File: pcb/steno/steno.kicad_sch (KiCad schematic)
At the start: 53 parts, among them J1 Conn_01x04, K1 diode-choc, K10 diode-choc, K11 diode-choc, K12 diode-choc, K13 diode-choc, K14 diode-choc, K15 diode-choc, K16 diode-choc, K17 diode-choc, K18 diode-choc, K19 diode-choc, K2 diode-choc, K20 diode-choc, K21 diode-choc, K22 diode-choc, K23 diode-choc, K24 diode-choc, K25 diode-choc, K26 diode-choc, K27 diode-choc, K28 diode-choc, K29 diode-choc, K3 diode-choc, K30 diode-choc, K4 diode-choc, K5 diode-choc, K6 diode-choc, K7 diode-choc, K8 diode-choc, K9 diode-choc, Q1 AO3401A, SW2 SW_Push, U1 MT25QL128ABA1ESE, U2 LCD2.2in, U3 Holyiot_18010_no_underside

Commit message: [pcb] Auklet 3
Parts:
- added K32, K33, K34, K35, K36, K38, K39, K40, K41, K42: diode-choc, pg1350:pg1350-D, symbol diode-choc:diode-choc
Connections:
- net C2: now also K32.2, K38.2
- net C3: now also K33.2, K39.2
- net C4: now also K34.2, K40.2
- net C5: now also K35.2, K41.2
- net C6: now also K36.2, K42.2
- net R3: now also K32.1, K33.1, K34.1, K35.1, K36.1; no longer K13.1, K14.1, K15.1, K16.1, K17.1, K18.1, U3.43 (P0.22)
- net R4: now also K13.1, K14.1, K15.1, K16.1, K17.1, K18.1, U3.43 (P0.22); no longer K19.1, K20.1, K21.1, K22.1, K23.1, K24.1, U3.41 ([L]_P1.03)
- net R5: now also K19.1, K20.1, K21.1, K22.1, K23.1, K24.1, U3.41 ([L]_P1.03); no longer K25.1, K26.1, K27.1, K28.1, K29.1, K30.1, U3.42 (P1.00)
- new net R6: K25.1, K26.1, K27.1, K28.1, K29.1, K30.1, U3.42 (P1.00)
- new net R7: K38.1, K39.1, K40.1, K41.1, K42.1
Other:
- moved on the sheet: K1, K10, K11, K12, K13, K14, K15, K16, K17, K18, K19, K2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

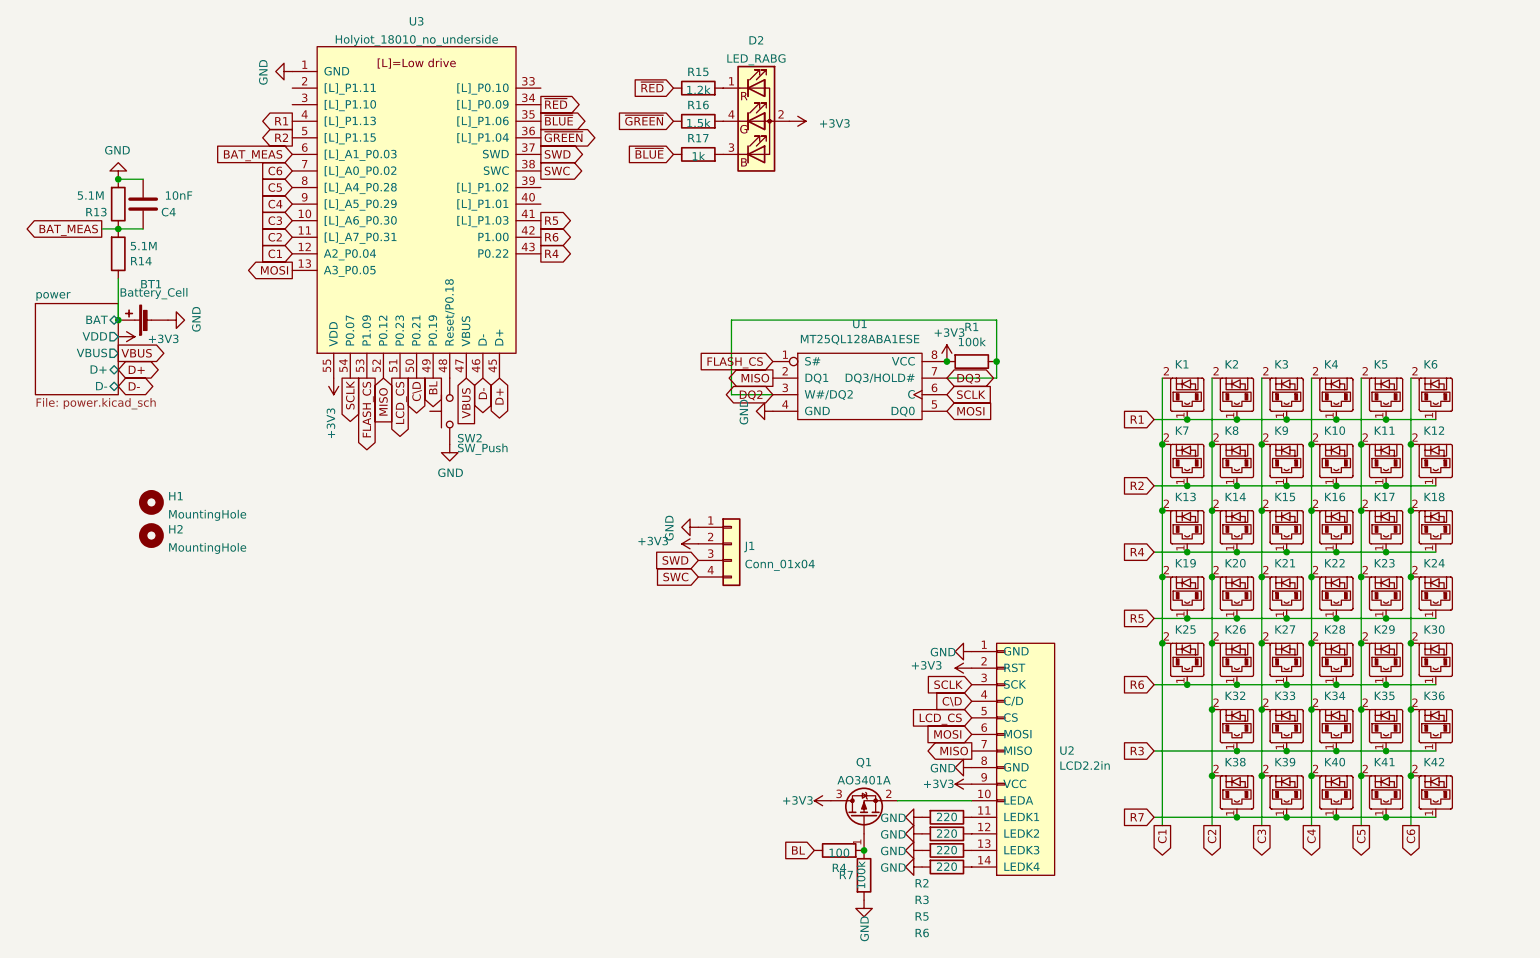
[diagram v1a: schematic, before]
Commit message: [pcb] auklet 3: use new libraries
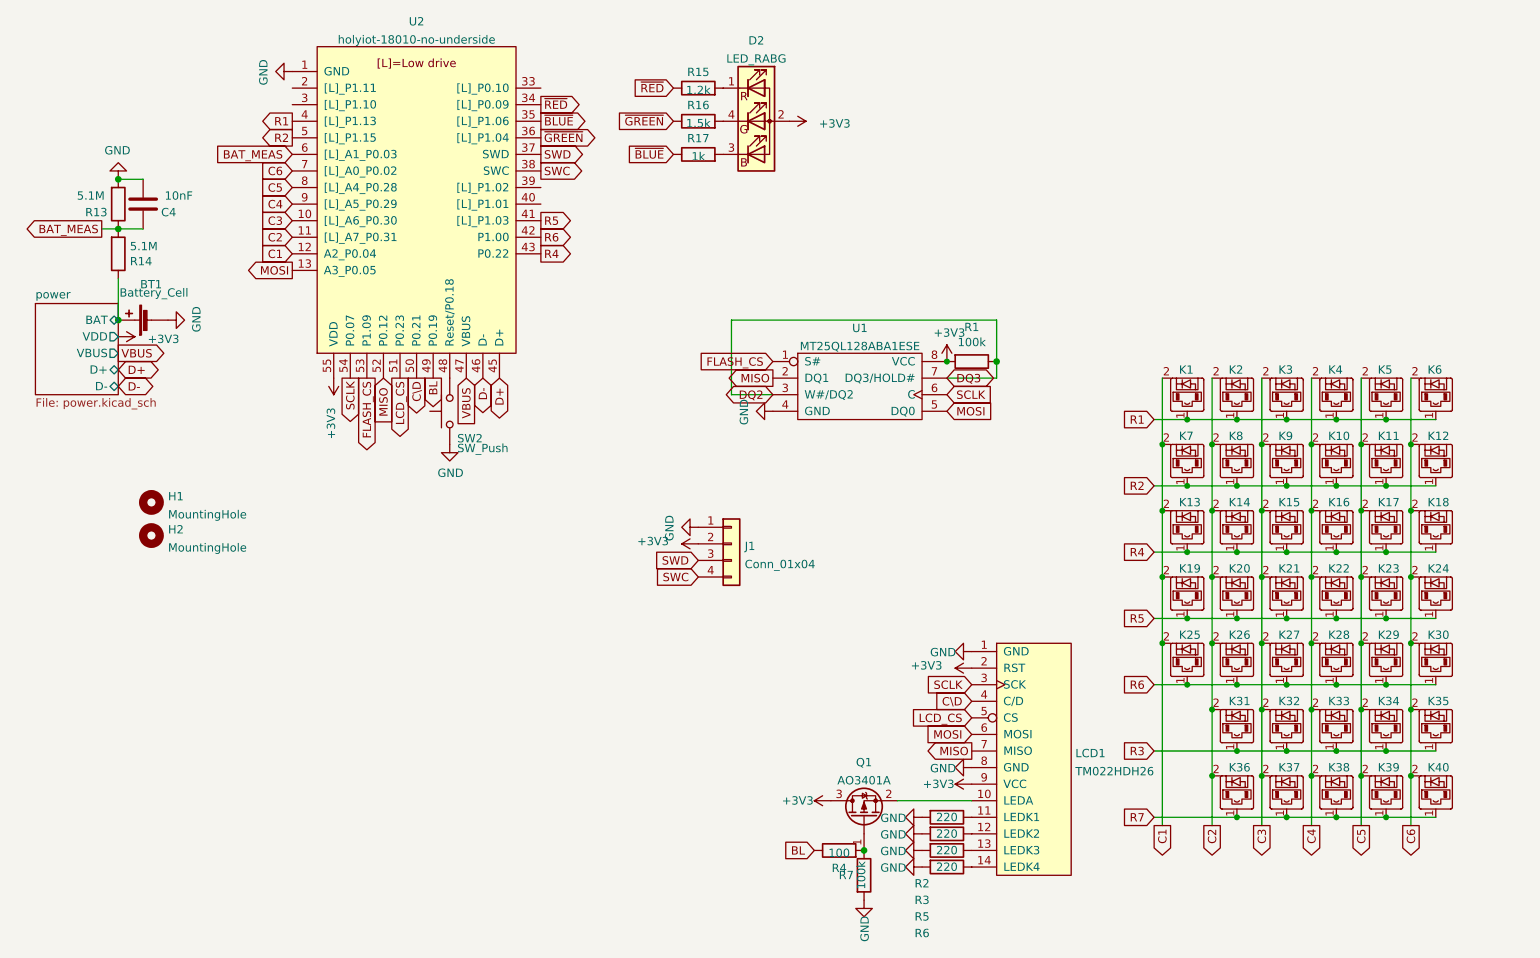
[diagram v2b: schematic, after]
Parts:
- removed K41, K42: diode-choc, pg1350:pg1350-D, symbol diode-choc:diode-choc
- removed U1: MT25QL128ABA1ESE, Package_SO:SOP-8_5.28x5.23mm_P1.27mm, symbol steno:MT25QL128ABA1ESE
- removed U2: LCD2.2in, misc:TM022HDH26, symbol steno:LCD2.2in
- removed U3: Holyiot_18010_no_underside, keeb-libs:Holyiot-18010-no-underside, symbol keeb-libs:Holyiot_18010_no_underside
- added K31, K37: diode-choc, pg1350:pg1350-D, symbol diode-choc:diode-choc
- added LCD1: TM022HDH26, display:TM022HDH26, symbol display:TM022HDH26
- added U1: MT25QL128ABA1ESE, Package_SO:SOIC-8_5.23x5.23mm_P1.27mm, symbol ic:MT25QL128ABA1ESE
- added U2: holyiot-18010-no-underside, mcu:Holyiot-18010-no-underside, symbol mcu:holyiot-18010-no-underside
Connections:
- net +3V3: now also LCD1.2 (RST), LCD1.9 (VCC), U1.8 (VCC), U2.55 (VDD)
- net BAT_MEAS: now also U2.6 ([L]_A1_P0.03)
- net BL: now also U2.49 (P0.19)
- net C1: now also U2.12 (A2_P0.04)
- net C2: now also K36.2, K31.2, U2.11 ([L]_A7_P0.31); no longer K32.2, K38.2
- net C3: now also K32.2, K37.2, U2.10 ([L]_A6_P0.30); no longer K33.2, K39.2
- net C4: now also K33.2, K38.2, U2.9 ([L]_A5_P0.29); no longer K34.2, K40.2
- net C5: now also K34.2, K39.2, U2.8 ([L]_A4_P0.28); no longer K35.2
- net C6: now also K35.2, K40.2, U2.7 ([L]_A0_P0.02); no longer K36.2
- net C\D: now also LCD1.4 (C/D), U2.50 (P0.21)
- net D+: now also U2.45 (D+)
- net D-: now also U2.46 (D-)
- net DQ2: now also U1.3 (W#/DQ2), U1.7 (DQ3/HOLD#)
- net FLASH_CS: now also U1.1 (S#), U2.53 (P1.09)
- net GND: now also LCD1.1 (GND), LCD1.8 (GND), U1.4 (GND), U2.1 (GND), U2.32 (GND), U2.44 (GND)
- net LCD_CS: now also LCD1.5 (CS), U2.51 (P0.23)
- net MISO: now also LCD1.7 (MISO), U1.2 (DQ1), U2.52 (P0.12)
- net MOSI: now also LCD1.6 (MOSI), U1.5 (DQ0), U2.13 (A3_P0.05)
- net R1: now also U2.4 ([L]_P1.13)
- net R2: now also U2.5 ([L]_P1.15)
- net R3: now also K31.1; no longer K36.1
- net R4: now also U2.43 (P0.22)
- net R5: now also U2.41 ([L]_P1.03)
- net R6: now also U2.42 (P1.00)
- net R7: now also K36.1, K37.1
- net SCLK: now also LCD1.3 (SCK), U1.6 (C), U2.54 (P0.07)
- net SWC: now also U2.38 (SWC)
- net SWD: now also U2.37 (SWD)
- net VBUS: now also U2.47 (VBUS)
- net ~{BLUE}: now also U2.35 ([L]_P1.06)
- net ~{GREEN}: now also U2.36 ([L]_P1.04)
- net ~{RED}: now also U2.34 ([L]_P0.09)
- net at Q1.2 (S): now also LCD1.10 (LEDA)
- net at R2.1: now also LCD1.11 (LEDK1)
- net at R3.1: now also LCD1.12 (LEDK2)
- net at R5.1: now also LCD1.13 (LEDK3)
- net at R6.1: now also LCD1.14 (LEDK4)
- net at SW2.2: now also U2.48 (Reset/P0.18)

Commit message: [pcb] Auklet 3: first revision
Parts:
- removed J1: Conn_01x04, keeb-libs:debug-port-single-side, symbol Connector_Generic:Conn_01x04
- added J1: debug-port, misc:debug-port-single-side, symbol misc:debug-port
- U2: footprint mcu:Holyiot-18010-no-underside -> mcu:holyiot-18010-no-underside
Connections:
- net +3V3: now also J1.2 (3V3)
- net GND: now also J1.1 (GND)
- net SWC: now also J1.4 (SWC)
- net SWD: now also J1.3 (SWD)
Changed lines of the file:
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@@
     )
   )
-  (global_label "SWD" (shape input) (at 119.38 110.49 180) (fields_autoplaced)
-    (effects (font (size 1.27 1.27)) (justify right))
-    (property "Intersheet References" "${INTERSHEET_REFS}" (id 0) (at 113.0359 110.4106 0)
-      (effects (font (size 1.27 1.27)) (justify right) hide)
-    )
-  )
-  (global_label "SWC" (shape input) (at 119.38 113.03 180) (fields_autoplaced)
-    (effects (font (size 1.27 1.27)) (justify right))
-    (property "Intersheet References" "${INTERSHEET_REFS}" (id 0) (at 113.0359 112.9506 0)
+  (global_label "SWD" (shape input) (at 128.27 120.65 180) (fields_autoplaced)
+    (effects (font (size 1.27 1.27)) (justify right))
+    (property "Intersheet References" "${INTERSHEET_REFS}" (id 0) (at 121.9259 120.5706 0)
+      (effects (font (size 1.27 1.27)) (justify right) hide)
+    )
+  )
+  (global_label "SWC" (shape input) (at 128.27 118.11 180) (fields_autoplaced)
+    (effects (font (size 1.27 1.27)) (justify right))
+    (property "Intersheet References" "${INTERSHEET_REFS}" (id 0) (at 121.9259 118.0306 0)
       (effects (font (size 1.27 1.27)) (justify right) hide)
     )
@@
     (pin "2")
   )
-  (symbol (lib_id "power:+3V3") (at 119.38 107.95 90) (unit 1)
-    (in_bom yes) (on_board yes)
-    (property "Reference" "#PWR06" (id 0) (at 123.19 107.95 0)
-      (effects (font (size 1.27 1.27)) hide)
-    )
-    (property "Value" "+3V3" (id 1) (at 112.4458 107.569 90))
-    (property "Footprint" "" (id 2) (at 119.38 107.95 0)
-      (effects (font (size 1.27 1.27)) hide)
-    )
-    (property "Datasheet" "" (id 3) (at 119.38 107.95 0)
+  (symbol (lib_id "power:+3V3") (at 128.27 123.19 90) (unit 1)
+    (in_bom yes) (on_board yes)
+    (property "Reference" "#PWR06" (id 0) (at 132.08 123.19 0)
+      (effects (font (size 1.27 1.27)) hide)
+    )
+    (property "Value" "+3V3" (id 1) (at 121.3358 122.809 90))
+    (property "Footprint" "" (id 2) (at 128.27 123.19 0)
+      (effects (font (size 1.27 1.27)) hide)
+    )
+    (property "Datasheet" "" (id 3) (at 128.27 123.19 0)
       (effects (font (size 1.27 1.27)) hide)
     )
@@
     (property "Reference" "U2" (id 0) (at 76.2 27.9105 0))
     (property "Value" "holyiot-18010-no-underside" (id 1) (at 76.2 30.6856 0))
-    (property "Footprint" "mcu:Holyiot-18010-no-underside" (id 2) (at 114.3 73.66 0)
+    (property "Footprint" "mcu:holyiot-18010-no-underside" (id 2) (at 114.3 73.66 0)
       (effects (font (size 1.27 1.27)) hide)
     )
@@
     (pin "2")
   )
-  (symbol (lib_id "power:GND") (at 119.38 105.41 270) (unit 1)
-    (in_bom yes) (on_board yes)
-    (property "Reference" "#PWR05" (id 0) (at 113.03 105.41 0)
-      (effects (font (size 1.27 1.27)) hide)
-    )
-    (property "Value" "GND" (id 1) (at 114.9858 105.537 0))
-    (property "Footprint" "" (id 2) (at 119.38 105.41 0)
-      (effects (font (size 1.27 1.27)) hide)
-    )
-    (property "Datasheet" "" (id 3) (at 119.38 105.41 0)
+  (symbol (lib_id "misc:debug-port") (at 132.08 121.92 90) (unit 1)
+    (in_bom no) (on_board yes) (fields_autoplaced)
+    (property "Reference" "J1" (id 0) (at 136.525 121.0115 90)
+      (effects (font (size 1.27 1.27)) (justify right))
+    )
+    (property "Value" "debug-port" (id 1) (at 136.525 123.7866 90)
+      (effects (font (size 1.27 1.27)) (justify right))
+    )
+    (property "Footprint" "misc:debug-port-single-side" (id 2) (at 139.7 121.92 0)
+      (effects (font (size 1.27 1.27)) hide)
+    )
+    (property "Datasheet" "" (id 3) (at 132.08 121.92 0)
+      (effects (font (size 1.27 1.27)) hide)
+    )
+    (pin "1")
+    (pin "2")
+    (pin "3")
+    (pin "4")
+  )
+  (symbol (lib_id "power:GND") (at 128.27 125.73 270) (unit 1)
+    (in_bom yes) (on_board yes)
+    (property "Reference" "#PWR05" (id 0) (at 121.92 125.73 0)
+      (effects (font (size 1.27 1.27)) hide)
+    )
+    (property "Value" "GND" (id 1) (at 123.8758 125.857 0))
+    (property "Footprint" "" (id 2) (at 128.27 125.73 0)
+      (effects (font (size 1.27 1.27)) hide)
+    )
+    (property "Datasheet" "" (id 3) (at 128.27 125.73 0)
       (effects (font (size 1.27 1.27)) hide)
     )
@@
     (pin "1")
     (pin "2")
-  )
-  (symbol (lib_id "Connector_Generic:Conn_01x04") (at 124.46 107.95 0) (unit 1)
-    (in_bom yes) (on_board yes) (fields_autoplaced)
-    (property "Reference" "J1" (id 0) (at 126.4921 108.3115 0)
-      (effects (font (size 1.27 1.27)) (justify left))
-    )
-    (property "Value" "Conn_01x04" (id 1) (at 126.4921 111.0866 0)
-      (effects (font (size 1.27 1.27)) (justify left))
-    )
-    (property "Footprint" "keeb-libs:debug-port-single-side" (id 2) (at 124.46 107.95 0)
-      (effects (font (size 1.27 1.27)) hide)
-    )
-    (property "Datasheet" "~" (id 3) (at 124.46 107.95 0)
-      (effects (font (size 1.27 1.27)) hide)
-    )
-    (pin "1")
-    (pin "2")
-    (pin "3")
-    (pin "4")
   )
   (symbol (lib_id "Device:Battery_Cell") (at 35.56 73.66 90) (unit 1)
@@
       (reference "H2") (unit 1) (value "MountingHole") (footprint "misc:auklet-cover-mount")
     )
-    (path "/847ba160-b305-4501-94eb-1e40ac133731"
-      (reference "J1") (unit 1) (value "Conn_01x04") (footprint "keeb-libs:debug-port-single-side")
+    (path "/51f1c228-b893-4ab5-bdfa-2eae1932a96d"
+      (reference "J1") (unit 1) (value "debug-port") (footprint "misc:debug-port-single-side")
     )
     (path "/144bad29-9f29-444f-a7e7-dc1674e796e3/9cfa9adb-81c6-4c01-b5f5-5a8080a68a7c"
@@
     )
     (path "/2086f1f4-059c-4ac4-858b-c6e65c5b1092"
-      (reference "U2") (unit 1) (value "holyiot-18010-no-underside") (footprint "mcu:Holyiot-18010-no-underside")
+      (reference "U2") (unit 1) (value "holyiot-18010-no-underside") (footprint "mcu:holyiot-18010-no-underside")
     )
     (path "/144bad29-9f29-444f-a7e7-dc1674e796e3/70f4f660-4e28-4704-85fb-b723fc879f87"
